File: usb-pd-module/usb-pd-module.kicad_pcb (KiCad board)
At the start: 2 copper layers, 34.3 x 46.3 mm, 36 parts, among them J1 USBC, J2 OUT, Q1 AO3407A, U1 CH221K, U2 SPX1117M3

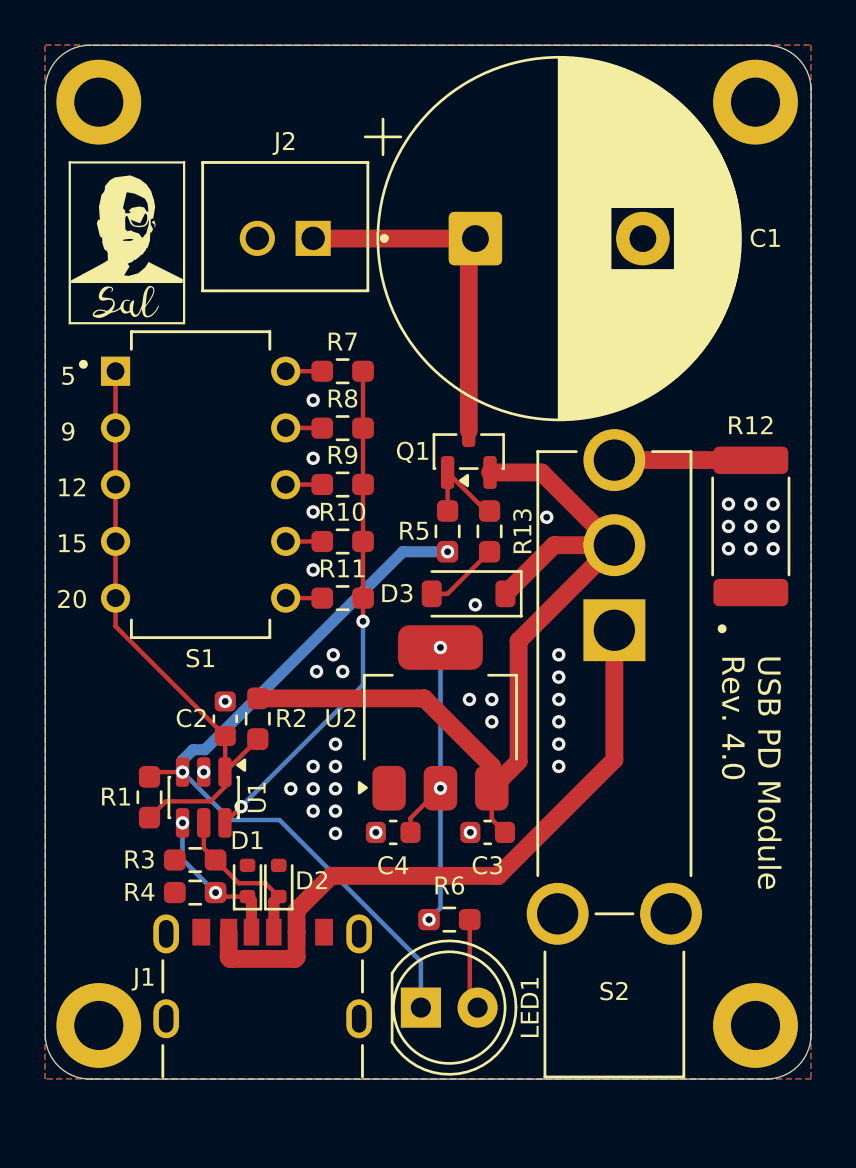
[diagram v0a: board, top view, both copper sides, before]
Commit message: Update USB PD Module to Rev 4.5 with improved power path and RGB LED indicator
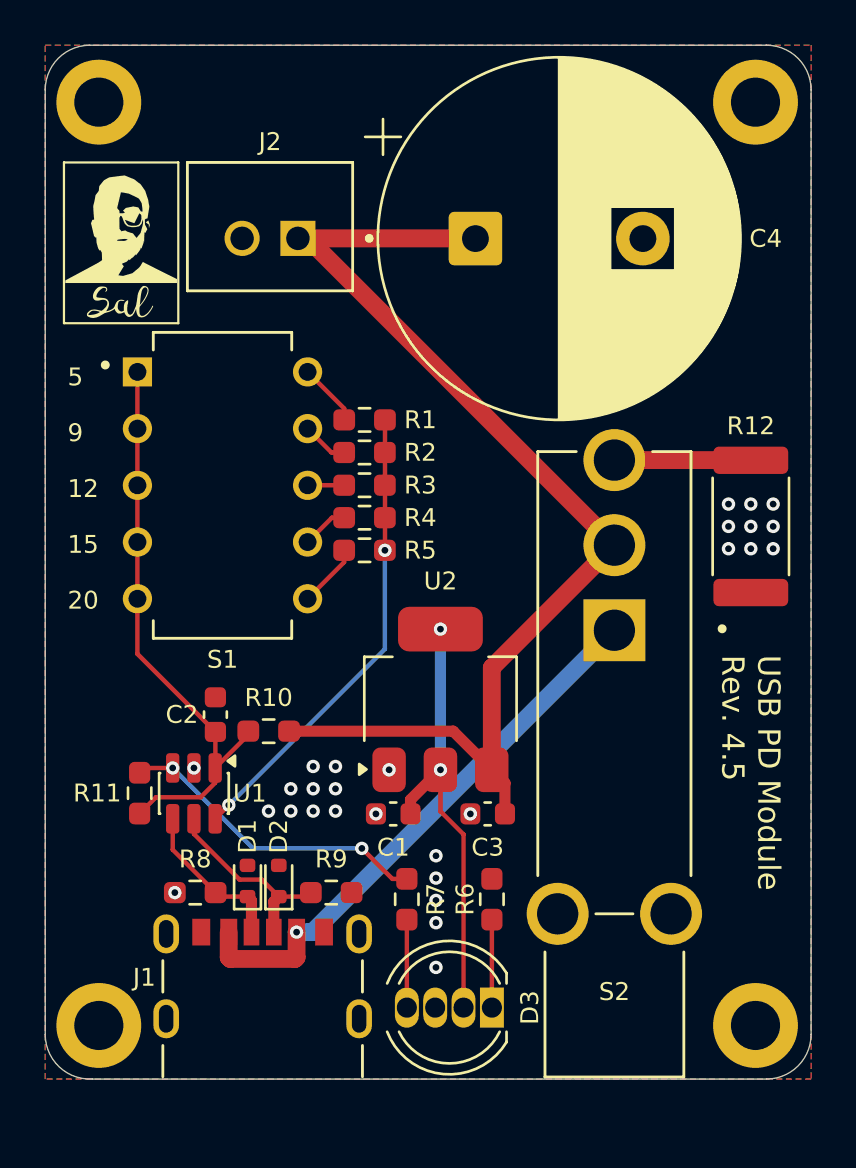
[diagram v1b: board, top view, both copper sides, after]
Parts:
- removed LED1: LED, LED_THT:LED_D5.0mm
- removed Q1: AO3407A, Package_TO_SOT_SMD:SOT-23
- removed R13: 100k, Resistor_SMD:R_0603_1608Metric_Pad0.98x0.95mm_HandSolder
- removed the R5 at (53.0, 63.5)
- added R7: 27, Resistor_SMD:R_0603_1608Metric_Pad0.98x0.95mm_HandSolder, F.Cu at (51.2, 79.9)
- D3: value 1N4148W -> RGB LED; footprint Diode_SMD:D_SOD-123 -> LED_THT:LED_D5.0mm-4_RGB
- R6: value 27 -> 150
- moved D3 18.6 mm to (55.0, 84.8)
- moved R9 6.26 mm to (47.8, 79.7), turned to 0 degrees
- moved REF** 6.18 mm to (59.6, 74.2)
- moved REF** 6.18 mm to (50.6, 74.0)
- moved R1 2.39 mm to (49.3, 58.5)
- moved R5 2.35 mm to (49.3, 64.3)
- moved R6 2.11 mm to (55.0, 79.9), turned to 90 degrees
- moved R2 1.47 mm to (49.3, 59.9)
- moved R4 1.45 mm to (49.3, 62.9)
- moved R3 0.98 mm to (49.3, 61.4)
- moved S1 0.98 mm to (42.9, 61.4)
- moved C1 0.83 mm to (50.6, 76.1)
- moved C3 0.83 mm to (54.8, 76.1)
- moved U2 0.83 mm to (52.7, 71.0)
- moved R10 0.74 mm to (45.0, 72.4), turned to 180 degrees
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- renumbered C4 to C1, C1 to C4, R7 to R1, R2 to R10, R1 to R11, R8 to R2, R9 to R3, R10 to R4, R11 to R5, R4 to R8, R3 to R9
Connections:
- C1 pad 2: Net-(U2-VOUT) -> Net-(D3-A)
- C4 pad 1: Net-(Q1-D) -> PWR
- D3 pad 1: PWR -> Net-(D3-RK)
- J2 pad 1: Net-(Q1-D) -> PWR
- R6 pad 1: Net-(U2-VOUT) -> Net-(D3-RK)
- R6 pad 2: Net-(LED1-A) -> GND
- U2 pad 2: Net-(U2-VOUT) -> Net-(D3-A)
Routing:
- net PG: track 34.1 -> 14.1 mm
- net Net-(D3-A): track 3.37 -> 19.9 mm, vias 0 -> 2
- net Net-(Q1-D): track 16.0 -> 0.00 mm
- net Net-(U2-VOUT): track 14.9 -> 0.00 mm, vias 3 -> 0
- net PWR: track 41.1 -> 52.4 mm
- net Net-(Q1-G): track 4.32 -> 0.00 mm
- net Net-(LED1-A): track 4.09 -> 0.00 mm
- net VBUS: track 29.2 -> 25.2 mm, vias 0 -> 1
- net Net-(D3-RK): track 0.00 -> 3.94 mm
- net Net-(D3-BK): track 0.00 -> 3.94 mm
- net CFG OUT: track 22.8 -> 21.0 mm
- net CC2: track 7.07 -> 8.84 mm
- net Net-(R5-Pad1): track 1.64 -> 2.85 mm
- net Net-(R1-Pad1): track 1.64 -> 2.83 mm
- net CFG IN: track 26.7 -> 26.1 mm
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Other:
- board text added: "USB PD Module Rev. 4.5"
- board text removed: "USB PD Module Rev. 4.0"

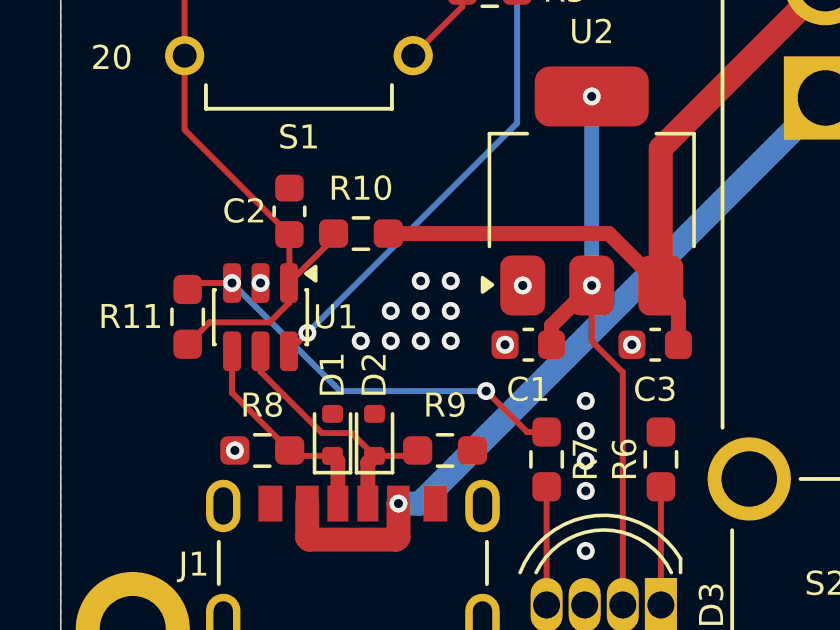
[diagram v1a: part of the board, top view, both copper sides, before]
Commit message: Update CH221K Pin Good path to LDO 3.3volts
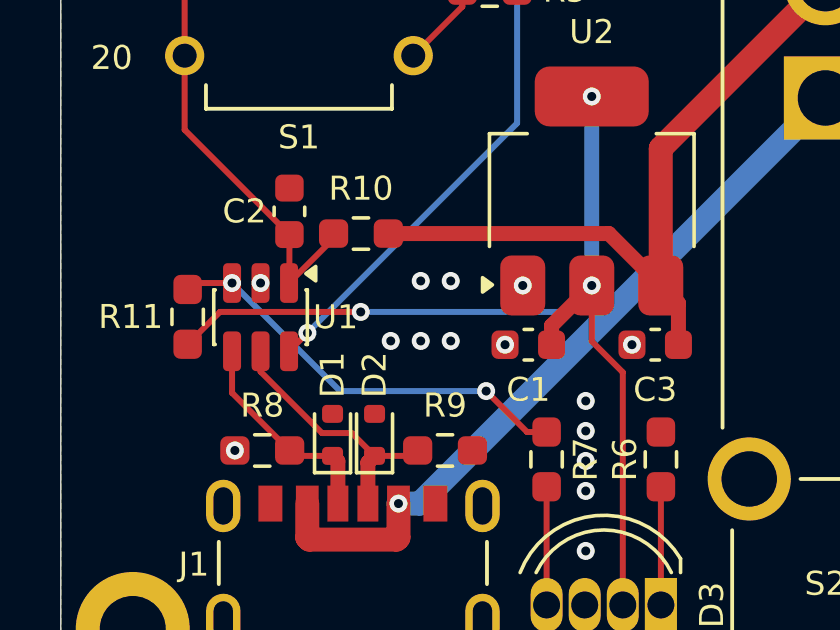
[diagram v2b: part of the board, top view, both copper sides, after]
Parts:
- R11: value 50k -> 10k
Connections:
- C1 pad 2: Net-(D3-A) -> LDO_OUT
- D3 pad 2: Net-(D3-A) -> LDO_OUT
- R11 pad 2: CFG IN -> LDO_OUT
- U2 pad 2: Net-(D3-A) -> LDO_OUT
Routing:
- net LDO_OUT: track 0.00 -> 34.2 mm, vias 0 -> 3
- net Net-(D3-A): track 19.9 -> 0.00 mm, vias 2 -> 0
- net CFG IN: track 26.1 -> 21.5 mm
- net GND: vias 28 -> 24
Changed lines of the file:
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@@
 	(net 13 "BLEED")
 	(net 14 "PG")
-	(net 15 "Net-(D3-A)")
+	(net 15 "LDO_OUT")
 	(net 16 "Net-(R3-Pad1)")
 	(net 17 "Net-(R4-Pad1)")
@@
 			)
 		)
-		(property "Value" "50k"
+		(property "Value" "10k"
 			(at 0 1.43 90)
 			(layer "F.Fab")
@@
 			(layers "F.Cu" "F.Mask" "F.Paste")
 			(roundrect_rratio 0.25)
-			(net 6 "CFG IN")
+			(net 15 "LDO_OUT")
 			(pintype "passive")
 		)
@@
 			(layers "F.Cu" "F.Mask" "F.Paste")
 			(roundrect_rratio 0.25)
-			(net 15 "Net-(D3-A)")
+			(net 15 "LDO_OUT")
 			(pintype "passive")
 		)
@@
 			(layers "F.Cu" "F.Mask" "F.Paste")
 			(roundrect_rratio 0.25)
-			(net 15 "Net-(D3-A)")
+			(net 15 "LDO_OUT")
 			(pinfunction "VOUT")
 			(pintype "power_out")
@@
 			(layers "F.Cu" "F.Mask" "F.Paste")
 			(roundrect_rratio 0.25)
-			(net 15 "Net-(D3-A)")
+			(net 15 "LDO_OUT")
 			(pinfunction "VOUT")
 			(pintype "power_out")
@@
 			(layers "*.Cu" "*.Mask")
 			(remove_unused_layers no)
-			(net 15 "Net-(D3-A)")
+			(net 15 "LDO_OUT")
 			(pinfunction "A")
 			(pintype "passive")
@@
 	)
 	(via
-		(at 48 74)
-		(size 0.6)
-		(drill 0.3)
-		(layers "F.Cu" "B.Cu")
-		(free yes)
-		(net 1)
-	)
-	(via
 		(at 50.4 74.15)
 		(size 0.6)
@@
 	)
 	(via
-		(at 46 76)
+		(at 48 74)
 		(size 0.6)
 		(drill 0.3)
@@
 	)
 	(via
-		(at 47 74)
-		(size 0.6)
-		(drill 0.3)
-		(layers "F.Cu" "B.Cu")
-		(free yes)
-		(net 1)
-	)
-	(via
 		(at 52.5 80)
 		(size 0.6)
@@
 	)
 	(via
-		(at 46 75)
-		(size 0.6)
-		(drill 0.3)
-		(layers "F.Cu" "B.Cu")
-		(free yes)
-		(net 1)
-	)
-	(via
-		(at 45 76)
+		(at 65.6 64.25)
 		(size 0.6)
 		(drill 0.3)
@@
 	)
 	(via
-		(at 48 75)
+		(at 40.805 79.65)
 		(size 0.6)
 		(drill 0.3)
 		(layers "F.Cu" "B.Cu")
-		(free yes)
 		(net 1)
 	)
 	(via
-		(at 65.6 64.25)
+		(at 47 74)
 		(size 0.6)
 		(drill 0.3)
@@
 	)
 	(via
-		(at 40.805 79.65)
-		(size 0.6)
-		(drill 0.3)
-		(layers "F.Cu" "B.Cu")
-		(net 1)
-	)
-	(via
 		(at 67.6 62.25)
 		(size 0.6)
@@
 	)
 	(via
-		(at 47 75)
+		(at 66.6 64.25)
 		(size 0.6)
 		(drill 0.3)
@@
 	)
 	(via
-		(at 66.6 64.25)
-		(size 0.6)
-		(drill 0.3)
-		(layers "F.Cu" "B.Cu")
-		(free yes)
-		(net 1)
-	)
-	(via
 		(at 66.6 63.25)
 		(size 0.6)
@@
 		(net 1)
 	)
+	(via
+		(at 46 76)
+		(size 0.6)
+		(drill 0.3)
+		(layers "F.Cu" "B.Cu")
+		(free yes)
+		(net 1)
+	)
 	(segment
 		(start 46.2575 81.42)
@@
 	)
 	(segment
-		(start 41.960999 75.38025)
-		(end 42.61 74.731249)
-		(width 0.2)
-		(layer "F.Cu")
-		(net 6)
-	)
-	(segment
-		(start 42.61 74.731249)
-		(end 42.61 74.06875)
-		(width 0.2)
-		(layer "F.Cu")
-		(net 6)
-	)
-	(segment
-		(start 39.23 76.10875)
-		(end 39.9585 75.38025)
-		(width 0.2)
-		(layer "F.Cu")
-		(net 6)
-	)
-	(segment
 		(start 42.61 74.06875)
 		(end 44.095 72.58375)
@@
 	)
 	(segment
-		(start 39.9585 75.38025)
-		(end 41.960999 75.38025)
-		(width 0.2)
-		(layer "F.Cu")
-		(net 6)
-	)
-	(segment
 		(start 42.6225 72.45375)
 		(end 42.6225 74.05625)
@@
 	)
 	(segment
+		(start 45 75.03225)
+		(end 40.3065 75.03225)
+		(width 0.2)
+		(layer "F.Cu")
+		(net 15)
+	)
+	(segment
+		(start 40.3065 75.03225)
+		(end 39.23 76.10875)
+		(width 0.2)
+		(layer "F.Cu")
+		(net 15)
+	)
+	(segment
 		(start 53.735 84.8)
 		(end 53.735 77.04511)
@@
 	)
 	(via
+		(at 45 75.03225)
+		(size 0.6)
+		(drill 0.3)
+		(layers "F.Cu" "B.Cu")
+		(net 15)
+	)
+	(via
 		(at 52.7 67.85)
 		(size 0.6)
@@
 	)
 	(segment
+		(start 45 75.03225)
+		(end 51.81775 75.03225)
+		(width 0.2)
+		(layer "B.Cu")
+		(net 15)
+	)
+	(segment
 		(start 52.7 74.15)
 		(end 52.7 67.85)
@@
 		(layer "B.Cu")
 		(net 15)
+	)
+	(segment
+		(start 51.81775 75.03225)
+		(end 52.7 74.15)
+		(width 0.2)
+		(layer "B.Cu")
+		(net 15)
